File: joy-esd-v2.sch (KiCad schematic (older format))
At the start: 4 parts, among them J1 DB9_Female, U1 ESDA6V3SC5, U2 ESDA6V3SC5

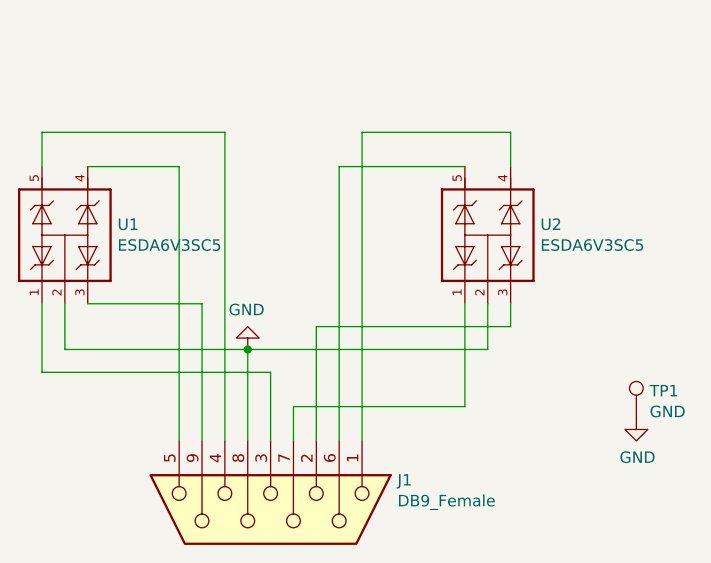
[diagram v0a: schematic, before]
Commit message: Move from 5 to 6 pin SOT-23 diodes
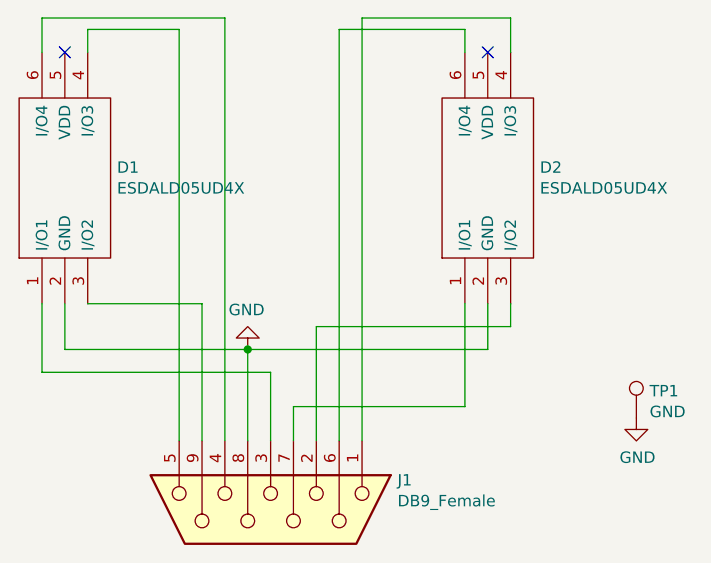
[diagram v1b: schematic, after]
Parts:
- removed U1, U2: ESDA6V3SC5, ESDA5V3SC5:SOT95P280X145-5N, symbol ESDA5V3SC5:ESDA5V3SC5
- added D1, D2: ESDALD05UD4X, SamacSys:SOT95P280X125-6N, symbol SamacSys_Parts:ESDALD05UD4X
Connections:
- net GND: now also D1.2 (GND), D2.2 (GND)
- net at J1.1: now also D2.4 (I/O3)
- net at J1.2: now also D2.3 (I/O2)
- net at J1.3: now also D1.1 (I/O1)
- net at J1.4: now also D1.6 (I/O4)
- net at J1.5: now also D1.4 (I/O3)
- net at J1.6: now also D2.6 (I/O4)
- net at J1.7: now also D2.1 (I/O1)
- net at J1.9: now also D1.3 (I/O2)
- no-connect marks 0 -> 2
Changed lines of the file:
@@
 	0    1    1    0
-$EndComp
-$Comp
-L ESDA5V3SC5:ESDA5V3SC5 U1
-U 1 1 603A45B2
-P 3900 2800
-F 0 "U1" V 3946 2570 50  0000 R CNN
-F 1 "ESDA6V3SC5" V 3855 2570 50  0000 R CNN
-F 2 "ESDA5V3SC5:SOT95P280X145-5N" H 3900 2800 50  0001 L BNN
-F 3 "" H 3900 2800 50  0001 L BNN
-F 4 "1.45mm" H 3900 2800 50  0001 L BNN "MAXIMUM_PACKAGE_HEIGHT"
-F 5 "IPC7351B" H 3900 2800 50  0001 L BNN "STANDARD"
-F 6 "10" H 3900 2800 50  0001 L BNN "PARTREV"
-F 7 "ST Microelectronics" H 3900 2800 50  0001 L BNN "MANUFACTURER"
-	1    3900 2800
-	0    -1   -1   0
-$EndComp
-$Comp
-L ESDA5V3SC5:ESDA5V3SC5 U2
-U 1 1 603AC0E0
-P 5750 2800
-F 0 "U2" V 5796 2570 50  0000 R CNN
-F 1 "ESDA6V3SC5" V 5705 2570 50  0000 R CNN
-F 2 "ESDA5V3SC5:SOT95P280X145-5N" H 5750 2800 50  0001 L BNN
-F 3 "" H 5750 2800 50  0001 L BNN
-F 4 "1.45mm" H 5750 2800 50  0001 L BNN "MAXIMUM_PACKAGE_HEIGHT"
-F 5 "IPC7351B" H 5750 2800 50  0001 L BNN "STANDARD"
-F 6 "10" H 5750 2800 50  0001 L BNN "PARTREV"
-F 7 "ST Microelectronics" H 5750 2800 50  0001 L BNN "MANUFACTURER"
-	1    5750 2800
-	0    -1   -1   0
 $EndComp
 Wire Wire Line
@@
 	4500 3100 4000 3100
 Wire Wire Line
-	4000 2500 4400 2500
-Wire Wire Line
-	4400 2500 4400 3700
-Wire Wire Line
 	3800 3100 3800 3400
 Wire Wire Line
@@
 Wire Wire Line
 	4800 3400 4800 3700
-Wire Wire Line
-	4600 3700 4600 2350
-Wire Wire Line
-	4600 2350 3800 2350
-Wire Wire Line
-	3800 2350 3800 2500
 Wire Wire Line
 	5650 3100 5650 3550
@@
 Wire Wire Line
 	4900 3550 4900 3700
-Wire Wire Line
-	5650 2500 5100 2500
-Wire Wire Line
-	5100 2500 5100 3700
-Wire Wire Line
-	5850 2500 5850 2350
-Wire Wire Line
-	5850 2350 5200 2350
-Wire Wire Line
-	5200 2350 5200 3700
 Wire Wire Line
 	5000 3700 5000 3200
@@
 	1    0    0    -1
 $EndComp
+$Comp
+L SamacSys_Parts:ESDALD05UD4X D1
+U 1 1 6248BDD5
+P 3800 3100
+F 0 "D1" V 4396 2772 50  0000 R CNN
+F 1 "ESDALD05UD4X" V 4305 2772 50  0000 R CNN
+F 2 "SamacSys:SOT95P280X125-6N" H 4750 3200 50  0001 L CNN
+F 3 "https://www.ween-semi.com/sites/default/files/2021-05/ESDALD05UD4.pdf" H 4750 3100 50  0001 L CNN
+F 4 "ESD Suppressors / TVS Diodes protect voltage sensitive components from ESD and transient voltage events" H 4750 3000 50  0001 L CNN "Description"
+F 5 "1.25" H 4750 2900 50  0001 L CNN "Height"
+F 6 "771-ESDALD05UD4X" H 4750 2800 50  0001 L CNN "Mouser Part Number"
+F 7 "https://www.mouser.co.uk/ProductDetail/WeEn-Semiconductors/ESDALD05UD4X?qs=aP1CjGhiNiEdF7M4wGPYzQ%3D%3D" H 4750 2700 50  0001 L CNN "Mouser Price/Stock"
+F 8 "WeEn Semiconductors" H 4750 2600 50  0001 L CNN "Manufacturer_Name"
+F 9 "ESDALD05UD4X" H 4750 2500 50  0001 L CNN "Manufacturer_Part_Number"
+	1    3800 3100
+	0    -1   -1   0
+$EndComp
+Wire Wire Line
+	4600 1850 3800 1850
+Wire Wire Line
+	3800 1850 3800 2000
+Wire Wire Line
+	4600 1850 4600 3700
+Wire Wire Line
+	4400 1900 4000 1900
+Wire Wire Line
+	4000 1900 4000 2000
+Wire Wire Line
+	4400 1900 4400 3700
+$Comp
+L SamacSys_Parts:ESDALD05UD4X D2
+U 1 1 62496779
+P 5650 3100
+F 0 "D2" V 6246 2772 50  0000 R CNN
+F 1 "ESDALD05UD4X" V 6155 2772 50  0000 R CNN
+F 2 "SamacSys:SOT95P280X125-6N" H 6600 3200 50  0001 L CNN
+F 3 "https://www.ween-semi.com/sites/default/files/2021-05/ESDALD05UD4.pdf" H 6600 3100 50  0001 L CNN
+F 4 "ESD Suppressors / TVS Diodes protect voltage sensitive components from ESD and transient voltage events" H 6600 3000 50  0001 L CNN "Description"
+F 5 "1.25" H 6600 2900 50  0001 L CNN "Height"
+F 6 "771-ESDALD05UD4X" H 6600 2800 50  0001 L CNN "Mouser Part Number"
+F 7 "https://www.mouser.co.uk/ProductDetail/WeEn-Semiconductors/ESDALD05UD4X?qs=aP1CjGhiNiEdF7M4wGPYzQ%3D%3D" H 6600 2700 50  0001 L CNN "Mouser Price/Stock"
+F 8 "WeEn Semiconductors" H 6600 2600 50  0001 L CNN "Manufacturer_Name"
+F 9 "ESDALD05UD4X" H 6600 2500 50  0001 L CNN "Manufacturer_Part_Number"
+	1    5650 3100
+	0    -1   -1   0
+$EndComp
+Wire Wire Line
+	5200 1850 5850 1850
+Wire Wire Line
+	5850 1850 5850 2000
+Wire Wire Line
+	5200 1850 5200 3700
+Wire Wire Line
+	5650 2000 5650 1900
+Wire Wire Line
+	5650 1900 5100 1900
+Wire Wire Line
+	5100 1900 5100 3700
+NoConn ~ 5750 2000
+NoConn ~ 3900 2000
 $EndSCHEMATC
